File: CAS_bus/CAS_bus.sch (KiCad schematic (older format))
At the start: 2 parts

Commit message: Update Schematic blocks
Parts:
- gave numbers to parts that had none: 1
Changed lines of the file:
@@
 $Descr A4 11693 8268
 encoding utf-8
-Sheet 5 5
+Sheet 3 6
 Title ""
 Date ""
@@
 $EndDescr
 $Comp
-L star-common-lib:CAS_stacking J?
+L star-common-lib:CAS_stacking J5
 U 1 1 5EAEC344
 P 5150 2750
-F 0 "J?" H 5150 4017 50  0000 C CNN
+F 0 "J5" H 5150 4017 50  0000 C CNN
 F 1 "CAS_stacking" H 5150 3926 50  0000 C CNN
 F 2 "" H 5250 3700 50  0001 C CNN
@@
 $EndComp
 $Comp
-L star-common-lib:CAS_stacking J?
+L star-common-lib:CAS_stacking J5
 U 2 1 5EAF24C5
 P 5150 5350
-F 0 "J?" H 5150 6617 50  0000 C CNN
+F 0 "J5" H 5150 6617 50  0000 C CNN
 F 1 "CAS_stacking" H 5150 6526 50  0000 C CNN
 F 2 "" H 5250 6300 50  0001 C CNN
@@
 SPI0_nSS8
 $Comp
-L power:+5V #PWR?
+L power:+5V #PWR030
 U 1 1 5EAFC0A6
 P 4400 2000
-F 0 "#PWR?" H 4400 1850 50  0001 C CNN
+F 0 "#PWR030" H 4400 1850 50  0001 C CNN
 F 1 "+5V" V 4415 2128 50  0000 L CNN
 F 2 "" H 4400 2000 50  0001 C CNN
@@
 $EndComp
 $Comp
-L power:+5V #PWR?
+L power:+5V #PWR044
 U 1 1 5EAFC439
 P 5900 2000
-F 0 "#PWR?" H 5900 1850 50  0001 C CNN
+F 0 "#PWR044" H 5900 1850 50  0001 C CNN
 F 1 "+5V" V 5915 2128 50  0000 L CNN
 F 2 "" H 5900 2000 50  0001 C CNN
@@
 $EndComp
 $Comp
-L power:+3.3V #PWR?
+L power:+3.3V #PWR047
 U 1 1 5EAFC7C9
 P 5900 3500
-F 0 "#PWR?" H 5900 3350 50  0001 C CNN
+F 0 "#PWR047" H 5900 3350 50  0001 C CNN
 F 1 "+3.3V" V 5915 3628 50  0000 L CNN
 F 2 "" H 5900 3500 50  0001 C CNN
@@
 $EndComp
 $Comp
-L power:+3.3V #PWR?
+L power:+3.3V #PWR036
 U 1 1 5EAFCB48
 P 4400 3500
-F 0 "#PWR?" H 4400 3350 50  0001 C CNN
+F 0 "#PWR036" H 4400 3350 50  0001 C CNN
 F 1 "+3.3V" V 4415 3628 50  0000 L CNN
 F 2 "" H 4400 3500 50  0001 C CNN
@@
 $EndComp
 $Comp
-L power:+BATT #PWR?
+L power:+BATT #PWR038
 U 1 1 5EAFCF46
 P 4400 3700
-F 0 "#PWR?" H 4400 3550 50  0001 C CNN
+F 0 "#PWR038" H 4400 3550 50  0001 C CNN
 F 1 "+BATT" V 4415 3827 50  0000 L CNN
 F 2 "" H 4400 3700 50  0001 C CNN
@@
 $EndComp
 $Comp
-L power:+BATT #PWR?
+L power:+BATT #PWR049
 U 1 1 5EAFD5BD
 P 5900 3700
-F 0 "#PWR?" H 5900 3550 50  0001 C CNN
+F 0 "#PWR049" H 5900 3550 50  0001 C CNN
 F 1 "+BATT" V 5915 3828 50  0000 L CNN
 F 2 "" H 5900 3700 50  0001 C CNN
@@
 $EndComp
 $Comp
-L power:GND #PWR?
+L power:GND #PWR046
 U 1 1 5EAFD991
 P 5900 2500
-F 0 "#PWR?" H 5900 2250 50  0001 C CNN
+F 0 "#PWR046" H 5900 2250 50  0001 C CNN
 F 1 "GND" V 5905 2372 50  0000 R CNN
 F 2 "" H 5900 2500 50  0001 C CNN
@@
 $EndComp
 $Comp
-L power:GND #PWR?
+L power:GND #PWR032
 U 1 1 5EAFDD6C
 P 4400 2500
-F 0 "#PWR?" H 4400 2250 50  0001 C CNN
+F 0 "#PWR032" H 4400 2250 50  0001 C CNN
 F 1 "GND" V 4405 2372 50  0000 R CNN
 F 2 "" H 4400 2500 50  0001 C CNN
@@
 $EndComp
 $Comp
-L power:GND #PWR?
+L power:GND #PWR033
 U 1 1 5EAFE12E
 P 4400 3000
-F 0 "#PWR?" H 4400 2750 50  0001 C CNN
+F 0 "#PWR033" H 4400 2750 50  0001 C CNN
 F 1 "GND" V 4405 2872 50  0000 R CNN
 F 2 "" H 4400 3000 50  0001 C CNN
@@
 $EndComp
 $Comp
-L power:GND #PWR?
+L power:GND #PWR034
 U 1 1 5EAFE4EB
 P 4400 3200
-F 0 "#PWR?" H 4400 2950 50  0001 C CNN
+F 0 "#PWR034" H 4400 2950 50  0001 C CNN
 F 1 "GND" V 4405 3072 50  0000 R CNN
 F 2 "" H 4400 3200 50  0001 C CNN
@@
 $EndComp
 $Comp
-L power:GND #PWR?
+L power:GND #PWR037
 U 1 1 5EAFEC1B
 P 4400 3600
-F 0 "#PWR?" H 4400 3350 50  0001 C CNN
+F 0 "#PWR037" H 4400 3350 50  0001 C CNN
 F 1 "GND" V 4405 3472 50  0000 R CNN
 F 2 "" H 4400 3600 50  0001 C CNN
@@
 $EndComp
 $Comp
-L power:GND #PWR?
+L power:GND #PWR048
 U 1 1 5EAFEFF0
 P 5900 3600
-F 0 "#PWR?" H 5900 3350 50  0001 C CNN
+F 0 "#PWR048" H 5900 3350 50  0001 C CNN
 F 1 "GND" V 5905 3472 50  0000 R CNN
 F 2 "" H 5900 3600 50  0001 C CNN
@@
 	5750 2000 5900 2000
 $Comp
-L power:GND #PWR?
+L power:GND #PWR043
 U 1 1 5EB0043E
 P 5900 1900
-F 0 "#PWR?" H 5900 1650 50  0001 C CNN
+F 0 "#PWR043" H 5900 1650 50  0001 C CNN
 F 1 "GND" V 5905 1772 50  0000 R CNN
 F 2 "" H 5900 1900 50  0001 C CNN
@@
 $EndComp
 $Comp
-L power:GND #PWR?
+L power:GND #PWR045
 U 1 1 5EB00872
 P 5900 2100
-F 0 "#PWR?" H 5900 1850 50  0001 C CNN
+F 0 "#PWR045" H 5900 1850 50  0001 C CNN
 F 1 "GND" V 5905 1972 50  0000 R CNN
 F 2 "" H 5900 2100 50  0001 C CNN
@@
 $EndComp
 $Comp
-L power:GND #PWR?
+L power:GND #PWR029
 U 1 1 5EB00CA1
 P 4400 1900
-F 0 "#PWR?" H 4400 1650 50  0001 C CNN
+F 0 "#PWR029" H 4400 1650 50  0001 C CNN
 F 1 "GND" V 4405 1772 50  0000 R CNN
 F 2 "" H 4400 1900 50  0001 C CNN
@@
 $EndComp
 $Comp
-L power:GND #PWR?
+L power:GND #PWR031
 U 1 1 5EB01123
 P 4400 2100
-F 0 "#PWR?" H 4400 1850 50  0001 C CNN
+F 0 "#PWR031" H 4400 1850 50  0001 C CNN
 F 1 "GND" V 4405 1972 50  0000 R CNN
 F 2 "" H 4400 2100 50  0001 C CNN
@@
 $EndComp
 $Comp
-L power:GND #PWR?
+L power:GND #PWR035
 U 1 1 5EB01534
 P 4400 3400
-F 0 "#PWR?" H 4400 3150 50  0001 C CNN
+F 0 "#PWR035" H 4400 3150 50  0001 C CNN
 F 1 "GND" V 4405 3272 50  0000 R CNN
 F 2 "" H 4400 3400 50  0001 C CNN
@@
 SPIHS_nSS2
 $Comp
-L power:GND #PWR?
+L power:GND #PWR039
 U 1 1 5EB1964E
 P 4400 4500
-F 0 "#PWR?" H 4400 4250 50  0001 C CNN
+F 0 "#PWR039" H 4400 4250 50  0001 C CNN
 F 1 "GND" V 4405 4372 50  0000 R CNN
 F 2 "" H 4400 4500 50  0001 C CNN
@@
 $EndComp
 $Comp
-L power:GND #PWR?
+L power:GND #PWR040
 U 1 1 5EB19A77
 P 4400 4600
-F 0 "#PWR?" H 4400 4350 50  0001 C CNN
+F 0 "#PWR040" H 4400 4350 50  0001 C CNN
 F 1 "GND" V 4405 4472 50  0000 R CNN
 F 2 "" H 4400 4600 50  0001 C CNN
@@
 $EndComp
 $Comp
-L power:GND #PWR?
+L power:GND #PWR041
 U 1 1 5EB19EAC
 P 4400 4700
-F 0 "#PWR?" H 4400 4450 50  0001 C CNN
+F 0 "#PWR041" H 4400 4450 50  0001 C CNN
 F 1 "GND" V 4405 4572 50  0000 R CNN
 F 2 "" H 4400 4700 50  0001 C CNN
@@
 $EndComp
 $Comp
-L power:GND #PWR?
+L power:GND #PWR042
 U 1 1 5EB1A2ED
 P 4400 4900
-F 0 "#PWR?" H 4400 4650 50  0001 C CNN
+F 0 "#PWR042" H 4400 4650 50  0001 C CNN
 F 1 "GND" V 4405 4772 50  0000 R CNN
 F 2 "" H 4400 4900 50  0001 C CNN
@@
 $EndComp
 $Comp
-L power:GND #PWR?
+L power:GND #PWR050
 U 1 1 5EB1A73A
 P 5900 4400
-F 0 "#PWR?" H 5900 4150 50  0001 C CNN
+F 0 "#PWR050" H 5900 4150 50  0001 C CNN
 F 1 "GND" V 5905 4272 50  0000 R CNN
 F 2 "" H 5900 4400 50  0001 C CNN
@@
 $EndComp
 $Comp
-L power:GND #PWR?
+L power:GND #PWR051
 U 1 1 5EB1ABC9
 P 5900 4500
-F 0 "#PWR?" H 5900 4250 50  0001 C CNN
+F 0 "#PWR051" H 5900 4250 50  0001 C CNN
 F 1 "GND" V 5905 4372 50  0000 R CNN
 F 2 "" H 5900 4500 50  0001 C CNN
@@
 $EndComp
 $Comp
-L power:GND #PWR?
+L power:GND #PWR052
 U 1 1 5EB1B064
 P 5900 4700
-F 0 "#PWR?" H 5900 4450 50  0001 C CNN
+F 0 "#PWR052" H 5900 4450 50  0001 C CNN
 F 1 "GND" V 5905 4572 50  0000 R CNN
 F 2 "" H 5900 4700 50  0001 C CNN
@@
 $EndComp
 $Comp
-L power:GND #PWR?
+L power:GND #PWR053
 U 1 1 5EB1B50B
 P 5900 4800
-F 0 "#PWR?" H 5900 4550 50  0001 C CNN
+F 0 "#PWR053" H 5900 4550 50  0001 C CNN
 F 1 "GND" V 5905 4672 50  0000 R CNN
 F 2 "" H 5900 4800 50  0001 C CNN
@@
 $EndComp
 $Comp
-L power:GND #PWR?
+L power:GND #PWR054
 U 1 1 5EB1B9BE
 P 5900 4900
-F 0 "#PWR?" H 5900 4650 50  0001 C CNN
+F 0 "#PWR054" H 5900 4650 50  0001 C CNN
 F 1 "GND" V 5905 4772 50  0000 R CNN
 F 2 "" H 5900 4900 50  0001 C CNN
@@
 +3.3V
 $Comp
-L power:+3.3V #PWR?
+L power:+3.3V #PWR055
 U 1 1 5EB35B08
 P 7800 1850
-F 0 "#PWR?" H 7800 1700 50  0001 C CNN
+F 0 "#PWR055" H 7800 1700 50  0001 C CNN
 F 1 "+3.3V" H 7815 2023 50  0000 C CNN
 F 2 "" H 7800 1850 50  0001 C CNN
@@
 +BATT
 $Comp
-L power:+5V #PWR?
+L power:+5V #PWR056
 U 1 1 5EB368D5
 P 8250 1850
-F 0 "#PWR?" H 8250 1700 50  0001 C CNN
+F 0 "#PWR056" H 8250 1700 50  0001 C CNN
 F 1 "+5V" H 8265 2023 50  0000 C CNN
 F 2 "" H 8250 1850 50  0001 C CNN
@@
 $EndComp
 $Comp
-L power:+BATT #PWR?
+L power:+BATT #PWR057
 U 1 1 5EB37213
 P 8700 1850
-F 0 "#PWR?" H 8700 1700 50  0001 C CNN
+F 0 "#PWR057" H 8700 1700 50  0001 C CNN
 F 1 "+BATT" H 8715 2023 50  0000 C CNN
 F 2 "" H 8700 1850 50  0001 C CNN

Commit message: Update schematics
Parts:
- renumbered J5 to J6
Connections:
- no-connect marks 0 -> 26
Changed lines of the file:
@@
 $EndDescr
 $Comp
-L star-common-lib:CAS_stacking J5
+L star-common-lib:CAS_stacking J6
 U 1 1 5EAEC344
 P 5150 2750
-F 0 "J5" H 5150 4017 50  0000 C CNN
+F 0 "J6" H 5150 4017 50  0000 C CNN
 F 1 "CAS_stacking" H 5150 3926 50  0000 C CNN
 F 2 "" H 5250 3700 50  0001 C CNN
@@
 $EndComp
 $Comp
-L star-common-lib:CAS_stacking J5
+L star-common-lib:CAS_stacking J6
 U 2 1 5EAF24C5
 P 5150 5350
-F 0 "J5" H 5150 6617 50  0000 C CNN
+F 0 "J6" H 5150 6617 50  0000 C CNN
 F 1 "CAS_stacking" H 5150 6526 50  0000 C CNN
 F 2 "" H 5250 6300 50  0001 C CNN
@@
 SPI0_nSS8
 $Comp
-L power:+5V #PWR030
+L power:+5V #PWR050
 U 1 1 5EAFC0A6
 P 4400 2000
-F 0 "#PWR030" H 4400 1850 50  0001 C CNN
+F 0 "#PWR050" H 4400 1850 50  0001 C CNN
 F 1 "+5V" V 4415 2128 50  0000 L CNN
 F 2 "" H 4400 2000 50  0001 C CNN
@@
 $EndComp
 $Comp
-L power:+5V #PWR044
+L power:+5V #PWR064
 U 1 1 5EAFC439
 P 5900 2000
-F 0 "#PWR044" H 5900 1850 50  0001 C CNN
+F 0 "#PWR064" H 5900 1850 50  0001 C CNN
 F 1 "+5V" V 5915 2128 50  0000 L CNN
 F 2 "" H 5900 2000 50  0001 C CNN
@@
 $EndComp
 $Comp
-L power:+3.3V #PWR047
+L power:+3.3V #PWR067
 U 1 1 5EAFC7C9
 P 5900 3500
-F 0 "#PWR047" H 5900 3350 50  0001 C CNN
+F 0 "#PWR067" H 5900 3350 50  0001 C CNN
 F 1 "+3.3V" V 5915 3628 50  0000 L CNN
 F 2 "" H 5900 3500 50  0001 C CNN
@@
 $EndComp
 $Comp
-L power:+3.3V #PWR036
+L power:+3.3V #PWR056
 U 1 1 5EAFCB48
 P 4400 3500
-F 0 "#PWR036" H 4400 3350 50  0001 C CNN
+F 0 "#PWR056" H 4400 3350 50  0001 C CNN
 F 1 "+3.3V" V 4415 3628 50  0000 L CNN
 F 2 "" H 4400 3500 50  0001 C CNN
@@
 $EndComp
 $Comp
-L power:+BATT #PWR038
+L power:+BATT #PWR058
 U 1 1 5EAFCF46
 P 4400 3700
-F 0 "#PWR038" H 4400 3550 50  0001 C CNN
+F 0 "#PWR058" H 4400 3550 50  0001 C CNN
 F 1 "+BATT" V 4415 3827 50  0000 L CNN
 F 2 "" H 4400 3700 50  0001 C CNN
@@
 $EndComp
 $Comp
-L power:+BATT #PWR049
+L power:+BATT #PWR069
 U 1 1 5EAFD5BD
 P 5900 3700
-F 0 "#PWR049" H 5900 3550 50  0001 C CNN
+F 0 "#PWR069" H 5900 3550 50  0001 C CNN
 F 1 "+BATT" V 5915 3828 50  0000 L CNN
 F 2 "" H 5900 3700 50  0001 C CNN
@@
 $EndComp
 $Comp
-L power:GND #PWR046
+L power:GND #PWR066
 U 1 1 5EAFD991
 P 5900 2500
-F 0 "#PWR046" H 5900 2250 50  0001 C CNN
+F 0 "#PWR066" H 5900 2250 50  0001 C CNN
 F 1 "GND" V 5905 2372 50  0000 R CNN
 F 2 "" H 5900 2500 50  0001 C CNN
@@
 $EndComp
 $Comp
-L power:GND #PWR032
+L power:GND #PWR052
 U 1 1 5EAFDD6C
 P 4400 2500
-F 0 "#PWR032" H 4400 2250 50  0001 C CNN
+F 0 "#PWR052" H 4400 2250 50  0001 C CNN
 F 1 "GND" V 4405 2372 50  0000 R CNN
 F 2 "" H 4400 2500 50  0001 C CNN
@@
 $EndComp
 $Comp
-L power:GND #PWR033
+L power:GND #PWR053
 U 1 1 5EAFE12E
 P 4400 3000
-F 0 "#PWR033" H 4400 2750 50  0001 C CNN
+F 0 "#PWR053" H 4400 2750 50  0001 C CNN
 F 1 "GND" V 4405 2872 50  0000 R CNN
 F 2 "" H 4400 3000 50  0001 C CNN
@@
 $EndComp
 $Comp
-L power:GND #PWR034
+L power:GND #PWR054
 U 1 1 5EAFE4EB
 P 4400 3200
-F 0 "#PWR034" H 4400 2950 50  0001 C CNN
+F 0 "#PWR054" H 4400 2950 50  0001 C CNN
 F 1 "GND" V 4405 3072 50  0000 R CNN
 F 2 "" H 4400 3200 50  0001 C CNN
@@
 $EndComp
 $Comp
-L power:GND #PWR037
+L power:GND #PWR057
 U 1 1 5EAFEC1B
 P 4400 3600
-F 0 "#PWR037" H 4400 3350 50  0001 C CNN
+F 0 "#PWR057" H 4400 3350 50  0001 C CNN
 F 1 "GND" V 4405 3472 50  0000 R CNN
 F 2 "" H 4400 3600 50  0001 C CNN
@@
 $EndComp
 $Comp
-L power:GND #PWR048
+L power:GND #PWR068
 U 1 1 5EAFEFF0
 P 5900 3600
-F 0 "#PWR048" H 5900 3350 50  0001 C CNN
+F 0 "#PWR068" H 5900 3350 50  0001 C CNN
 F 1 "GND" V 5905 3472 50  0000 R CNN
 F 2 "" H 5900 3600 50  0001 C CNN
@@
 	5750 2000 5900 2000
 $Comp
-L power:GND #PWR043
+L power:GND #PWR063
 U 1 1 5EB0043E
 P 5900 1900
-F 0 "#PWR043" H 5900 1650 50  0001 C CNN
+F 0 "#PWR063" H 5900 1650 50  0001 C CNN
 F 1 "GND" V 5905 1772 50  0000 R CNN
 F 2 "" H 5900 1900 50  0001 C CNN
@@
 $EndComp
 $Comp
-L power:GND #PWR045
+L power:GND #PWR065
 U 1 1 5EB00872
 P 5900 2100
-F 0 "#PWR045" H 5900 1850 50  0001 C CNN
+F 0 "#PWR065" H 5900 1850 50  0001 C CNN
 F 1 "GND" V 5905 1972 50  0000 R CNN
 F 2 "" H 5900 2100 50  0001 C CNN
@@
 $EndComp
 $Comp
-L power:GND #PWR029
+L power:GND #PWR049
 U 1 1 5EB00CA1
 P 4400 1900
-F 0 "#PWR029" H 4400 1650 50  0001 C CNN
+F 0 "#PWR049" H 4400 1650 50  0001 C CNN
 F 1 "GND" V 4405 1772 50  0000 R CNN
 F 2 "" H 4400 1900 50  0001 C CNN
@@
 $EndComp
 $Comp
-L power:GND #PWR031
+L power:GND #PWR051
 U 1 1 5EB01123
 P 4400 2100
-F 0 "#PWR031" H 4400 1850 50  0001 C CNN
+F 0 "#PWR051" H 4400 1850 50  0001 C CNN
 F 1 "GND" V 4405 1972 50  0000 R CNN
 F 2 "" H 4400 2100 50  0001 C CNN
@@
 $EndComp
 $Comp
-L power:GND #PWR035
+L power:GND #PWR055
 U 1 1 5EB01534
 P 4400 3400
-F 0 "#PWR035" H 4400 3150 50  0001 C CNN
+F 0 "#PWR055" H 4400 3150 50  0001 C CNN
 F 1 "GND" V 4405 3272 50  0000 R CNN
 F 2 "" H 4400 3400 50  0001 C CNN
@@
 SPIHS_nSS2
 $Comp
-L power:GND #PWR039
+L power:GND #PWR059
 U 1 1 5EB1964E
 P 4400 4500
-F 0 "#PWR039" H 4400 4250 50  0001 C CNN
+F 0 "#PWR059" H 4400 4250 50  0001 C CNN
 F 1 "GND" V 4405 4372 50  0000 R CNN
 F 2 "" H 4400 4500 50  0001 C CNN
@@
 $EndComp
 $Comp
-L power:GND #PWR040
+L power:GND #PWR060
 U 1 1 5EB19A77
 P 4400 4600
-F 0 "#PWR040" H 4400 4350 50  0001 C CNN
+F 0 "#PWR060" H 4400 4350 50  0001 C CNN
 F 1 "GND" V 4405 4472 50  0000 R CNN
 F 2 "" H 4400 4600 50  0001 C CNN
@@
 $EndComp
 $Comp
-L power:GND #PWR041
+L power:GND #PWR061
 U 1 1 5EB19EAC
 P 4400 4700
-F 0 "#PWR041" H 4400 4450 50  0001 C CNN
+F 0 "#PWR061" H 4400 4450 50  0001 C CNN
 F 1 "GND" V 4405 4572 50  0000 R CNN
 F 2 "" H 4400 4700 50  0001 C CNN
@@
 $EndComp
 $Comp
-L power:GND #PWR042
+L power:GND #PWR062
 U 1 1 5EB1A2ED
 P 4400 4900
-F 0 "#PWR042" H 4400 4650 50  0001 C CNN
+F 0 "#PWR062" H 4400 4650 50  0001 C CNN
 F 1 "GND" V 4405 4772 50  0000 R CNN
 F 2 "" H 4400 4900 50  0001 C CNN
@@
 $EndComp
 $Comp
-L power:GND #PWR050
+L power:GND #PWR070
 U 1 1 5EB1A73A
 P 5900 4400
-F 0 "#PWR050" H 5900 4150 50  0001 C CNN
+F 0 "#PWR070" H 5900 4150 50  0001 C CNN
 F 1 "GND" V 5905 4272 50  0000 R CNN
 F 2 "" H 5900 4400 50  0001 C CNN
@@
 $EndComp
 $Comp
-L power:GND #PWR051
+L power:GND #PWR071
 U 1 1 5EB1ABC9
 P 5900 4500
-F 0 "#PWR051" H 5900 4250 50  0001 C CNN
+F 0 "#PWR071" H 5900 4250 50  0001 C CNN
 F 1 "GND" V 5905 4372 50  0000 R CNN
 F 2 "" H 5900 4500 50  0001 C CNN
@@
 $EndComp
 $Comp
-L power:GND #PWR052
+L power:GND #PWR072
 U 1 1 5EB1B064
 P 5900 4700
-F 0 "#PWR052" H 5900 4450 50  0001 C CNN
+F 0 "#PWR072" H 5900 4450 50  0001 C CNN
 F 1 "GND" V 5905 4572 50  0000 R CNN
 F 2 "" H 5900 4700 50  0001 C CNN
@@
 $EndComp
 $Comp
-L power:GND #PWR053
+L power:GND #PWR073
 U 1 1 5EB1B50B
 P 5900 4800
-F 0 "#PWR053" H 5900 4550 50  0001 C CNN
+F 0 "#PWR073" H 5900 4550 50  0001 C CNN
 F 1 "GND" V 5905 4672 50  0000 R CNN
 F 2 "" H 5900 4800 50  0001 C CNN
@@
 $EndComp
 $Comp
-L power:GND #PWR054
+L power:GND #PWR074
 U 1 1 5EB1B9BE
 P 5900 4900
-F 0 "#PWR054" H 5900 4650 50  0001 C CNN
+F 0 "#PWR074" H 5900 4650 50  0001 C CNN
 F 1 "GND" V 5905 4772 50  0000 R CNN
 F 2 "" H 5900 4900 50  0001 C CNN
@@
 +3.3V
 $Comp
-L power:+3.3V #PWR055
+L power:+3.3V #PWR075
 U 1 1 5EB35B08
 P 7800 1850
-F 0 "#PWR055" H 7800 1700 50  0001 C CNN
+F 0 "#PWR075" H 7800 1700 50  0001 C CNN
 F 1 "+3.3V" H 7815 2023 50  0000 C CNN
 F 2 "" H 7800 1850 50  0001 C CNN
@@
 +BATT
 $Comp
-L power:+5V #PWR056
+L power:+5V #PWR076
 U 1 1 5EB368D5
 P 8250 1850
-F 0 "#PWR056" H 8250 1700 50  0001 C CNN
+F 0 "#PWR076" H 8250 1700 50  0001 C CNN
 F 1 "+5V" H 8265 2023 50  0000 C CNN
 F 2 "" H 8250 1850 50  0001 C CNN
@@
 $EndComp
 $Comp
-L power:+BATT #PWR057
+L power:+BATT #PWR077
 U 1 1 5EB37213
 P 8700 1850
-F 0 "#PWR057" H 8700 1700 50  0001 C CNN
+F 0 "#PWR077" H 8700 1700 50  0001 C CNN
 F 1 "+BATT" H 8715 2023 50  0000 C CNN
 F 2 "" H 8700 1850 50  0001 C CNN
@@
 Wire Wire Line
 	8700 2000 8700 1850
+NoConn ~ 4550 5100
+NoConn ~ 4550 5200
+NoConn ~ 4550 5300
+NoConn ~ 4550 5400
+NoConn ~ 4550 5500
+NoConn ~ 4550 5600
+NoConn ~ 4550 5700
+NoConn ~ 4550 5800
+NoConn ~ 4550 5900
+NoConn ~ 4550 6000
+NoConn ~ 4550 6100
+NoConn ~ 4550 6200
+NoConn ~ 4550 6300
+NoConn ~ 5750 6300
+NoConn ~ 5750 6200
+NoConn ~ 5750 6100
+NoConn ~ 5750 6000
+NoConn ~ 5750 5900
+NoConn ~ 5750 5800
+NoConn ~ 5750 5700
+NoConn ~ 5750 5600
+NoConn ~ 5750 5500
+NoConn ~ 5750 5400
+NoConn ~ 5750 5300
+NoConn ~ 5750 5200
+NoConn ~ 5750 5100
 $EndSCHEMATC

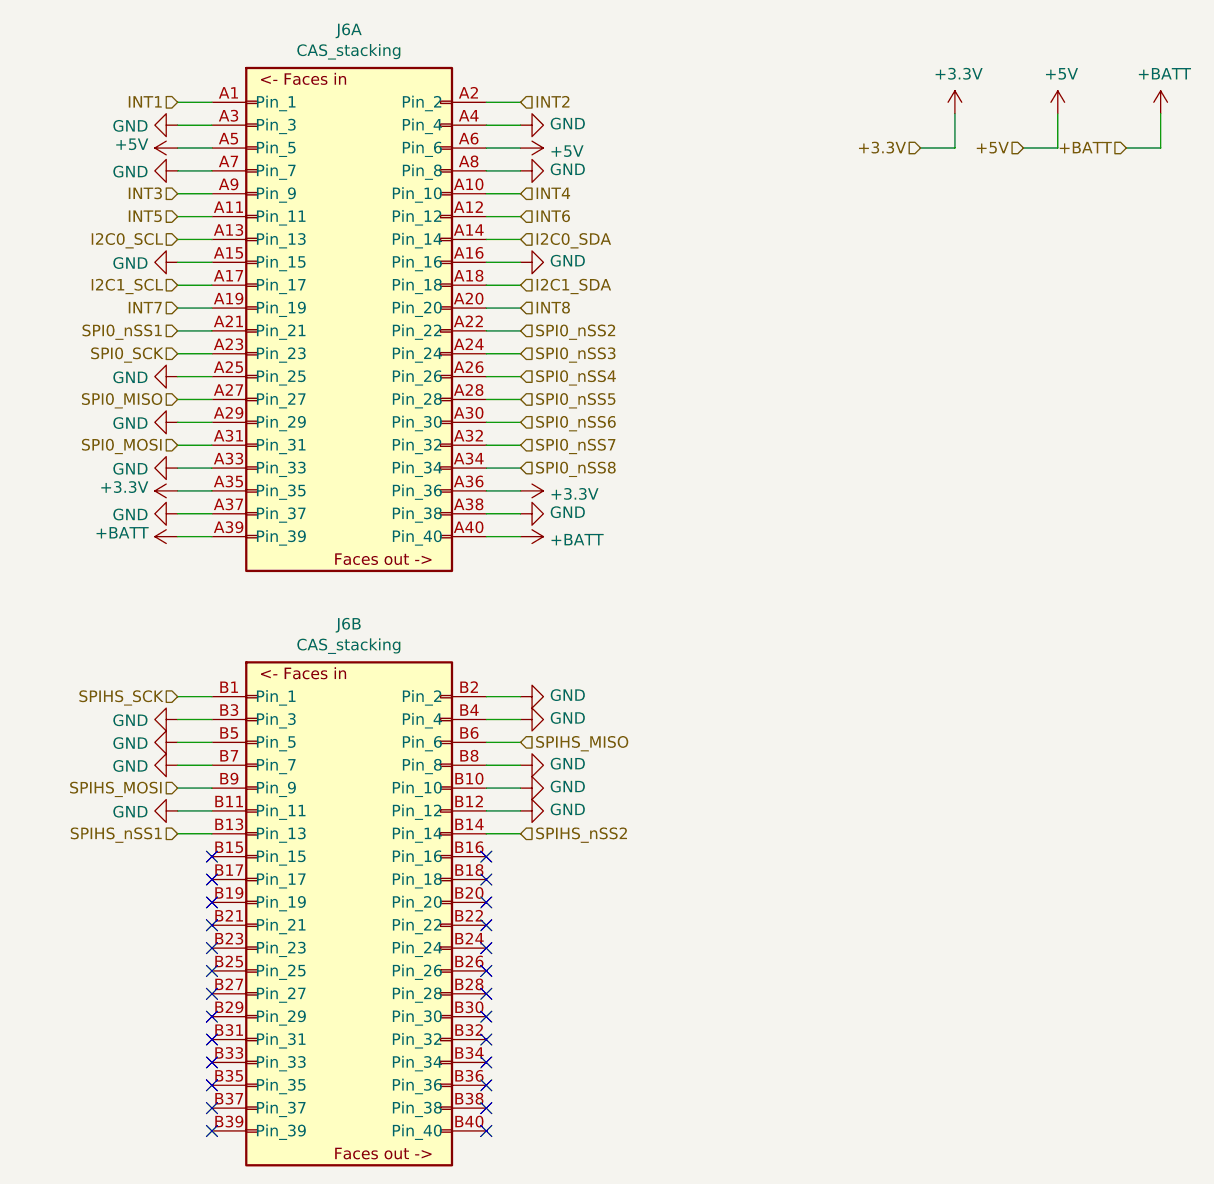
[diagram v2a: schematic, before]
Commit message: Revert schematics so that it can merge
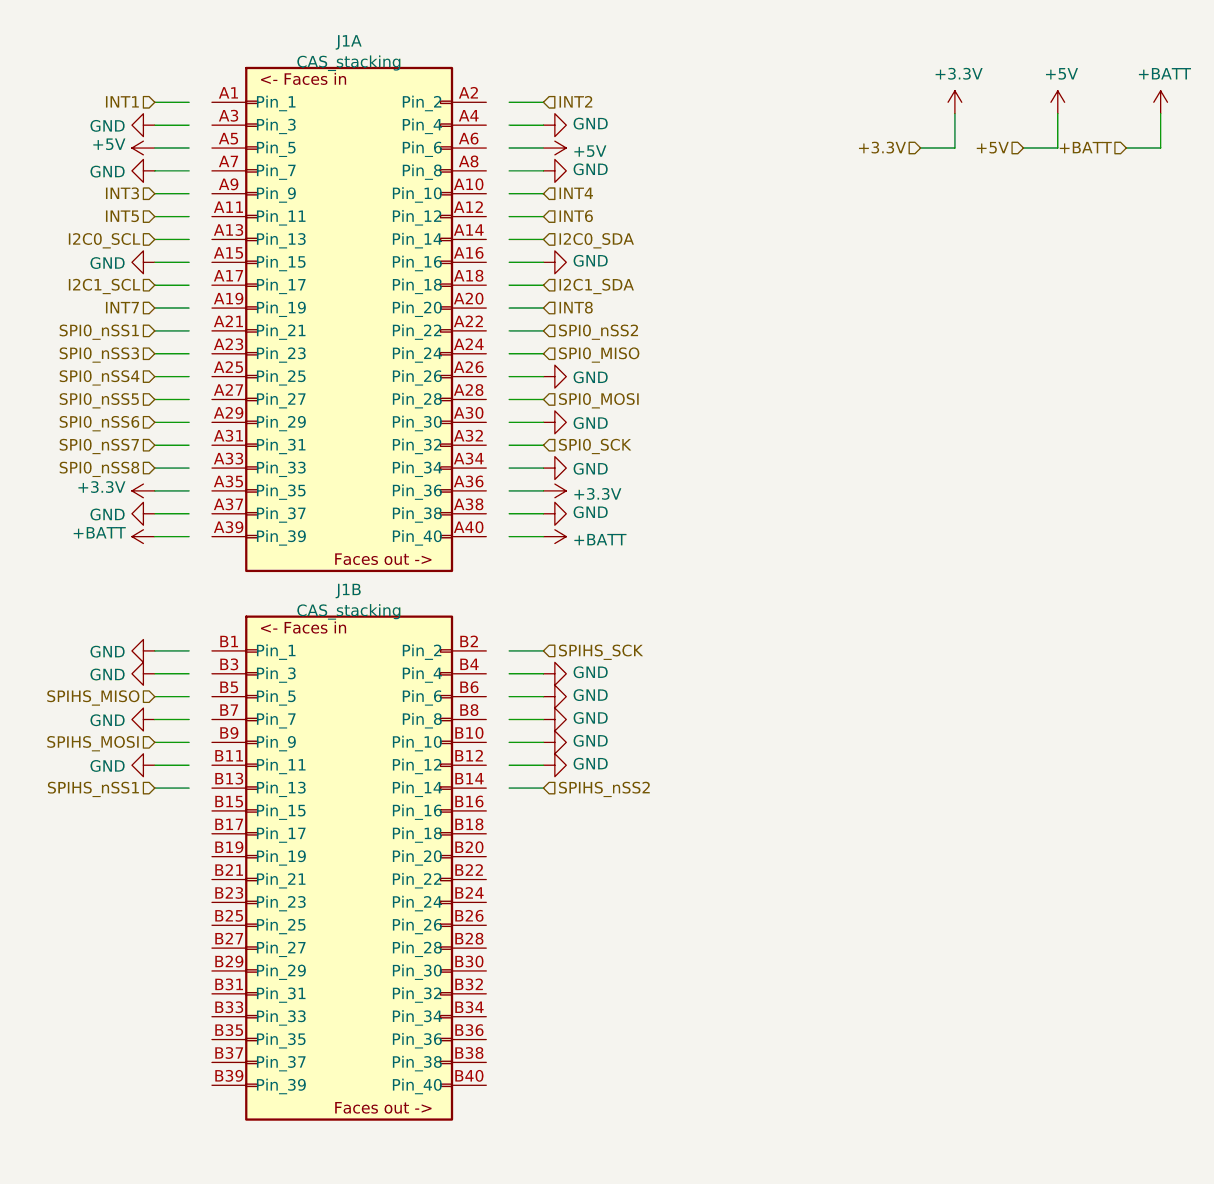
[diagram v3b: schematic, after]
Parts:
- removed J6: CAS_stacking, symbol star-common-lib:CAS_stacking
- added J1: CAS_stacking, symbol star-common-lib:CAS_stacking
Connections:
- no-connect marks 26 -> 0
